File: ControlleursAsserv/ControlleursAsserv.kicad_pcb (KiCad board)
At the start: 2 copper layers, 116 parts, among them J1 I2C1_5, J10 Codeur, J11 Motor FeedBack, J12 Motor CMD, J13 Codeur, J14 Motor FeedBack, J15 Motor CMD, J16 Codeur, J17 Motor FeedBack, J18 Motor CMD, J2 I2C2_5, J3 CAN1, J4 CAN2, J5 In App Prog, J6 DEBUG, J7 Codeur, J8 Motor CMD, J9 Motor FeedBack, Q1 BSS138, Q10 BSS138, Q11 BSS138, Q12 BSS138, Q13 BSS138, Q14 BSS138, Q2 BSS138, Q3 BSS138, Q4 BSS138, Q5 BSS138, Q6 BSS138, Q7 BSS138, Q8 BSS138, Q9 BSS138, SW1 RESET, SW2 BOOT0, U1 STM32G474RETx, U2 AMS1117-3.3, U3 MCP2558FD-xSN, Y1 16MHz

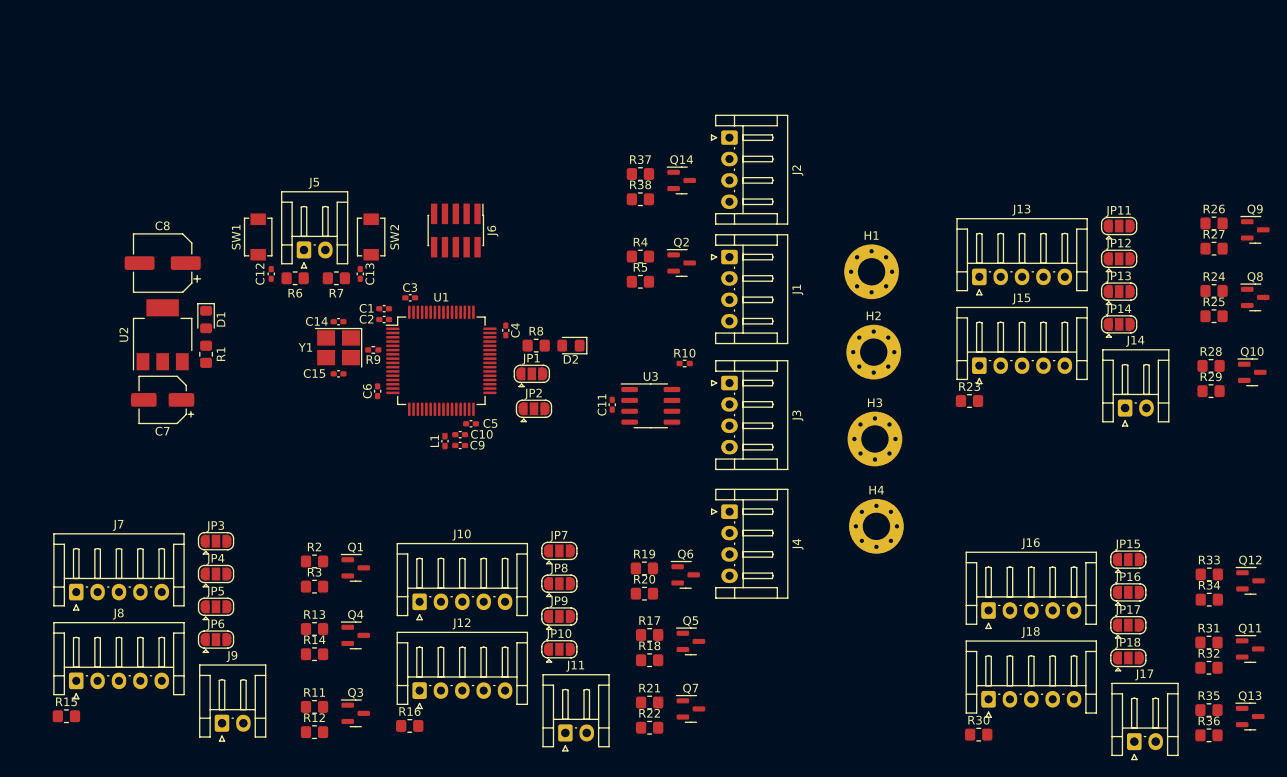
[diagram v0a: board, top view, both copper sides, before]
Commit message: Finalize placement for AsservController
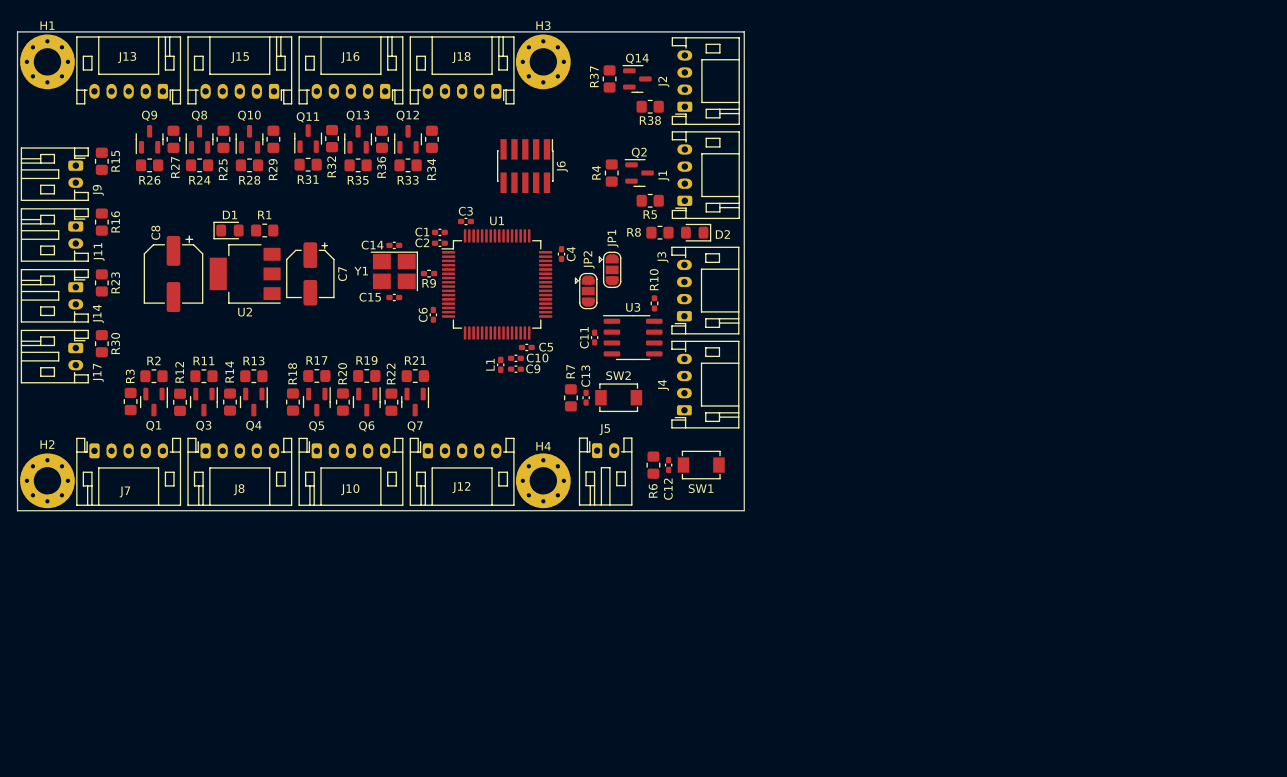
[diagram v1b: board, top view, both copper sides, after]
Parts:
- removed JP10, JP14, JP18, JP3: alim selector, Jumper:SolderJumper-3_P1.3mm_Open_RoundedPad1.0x1.5mm
- removed JP11, JP15, JP4, JP7: CHA Selector, Jumper:SolderJumper-3_P1.3mm_Open_RoundedPad1.0x1.5mm
- removed JP12, JP16, JP5, JP8: CHB Selector, Jumper:SolderJumper-3_P1.3mm_Open_RoundedPad1.0x1.5mm
- removed JP13, JP17, JP6, JP9: IDX Selector, Jumper:SolderJumper-3_P1.3mm_Open_RoundedPad1.0x1.5mm
- J1, J2, J3, J4: footprint Connector_JST:JST_EH_S4B-EH_1x04_P2.50mm_Horizontal -> Connector_JST:JST_PH_S4B-PH-K_1x04_P2.00mm_Horizontal
- J10, J12, J13, J15, J16, J18, J7, J8: footprint Connector_JST:JST_EH_S5B-EH_1x05_P2.50mm_Horizontal -> Connector_JST:JST_PH_S5B-PH-K_1x05_P2.00mm_Horizontal
- J11, J14, J17, J5, J9: footprint Connector_JST:JST_EH_S2B-EH_1x02_P2.50mm_Horizontal -> Connector_JST:JST_PH_S2B-PH-K_1x02_P2.00mm_Horizontal
- moved J17 132.1 mm to (67.6, 75.7), turned to -90 degrees
- moved Q9 129.7 mm to (76.2, 51.3), turned to 90 degrees
- moved Q11 125.3 mm to (94.7, 51.2), turned to 90 degrees
- moved Q8 124.9 mm to (82.0, 51.3), turned to 90 degrees
- moved R26 124.7 mm to (76.2, 54.4)
- moved Q13 124.3 mm to (100.6, 51.3), turned to 90 degrees
- moved J14 123.5 mm to (67.6, 68.6), turned to -90 degrees
- moved R27 122.4 mm to (79.0, 51.3), turned to 90 degrees
- moved Q10 120.4 mm to (87.9, 51.3), turned to 90 degrees
- moved R32 119.8 mm to (97.5, 51.2), turned to 90 degrees
- moved R24 119.6 mm to (82.0, 54.4)
- moved R31 119.3 mm to (94.7, 54.3)
- moved R36 119.2 mm to (103.4, 51.3), turned to 90 degrees
- moved R35 118.2 mm to (100.6, 54.4)
- moved R25 117.7 mm to (84.8, 51.3), turned to 90 degrees
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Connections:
- J10 pad 1: Net-(J10-Pin_1) -> +5V
- J13 pad 1: Net-(J13-Pin_1) -> +5V
- J16 pad 1: Net-(J16-Pin_1) -> +5V
- J7 pad 1: Net-(J7-Pin_1) -> +5V
- Q1 pad 2: /Codeur_Moteur_1/CHA Shifter/LV -> CHA_1
- Q10 pad 2: /Codeur_Moteur_3/CHA Shifter/LV -> CHA_3
- Q11 pad 2: /Codeur_Moteur_4/IDX Shifter/LV -> IDX_4
- Q12 pad 2: /Codeur_Moteur_4/CHA Shifter/LV -> CHA_4
- Q13 pad 2: /Codeur_Moteur_4/CHB Shifter/LV -> CHB_4
- Q3 pad 2: /Codeur_Moteur_1/CHB Shifter/LV -> CHB_1
- Q4 pad 2: /Codeur_Moteur_1/IDX Shifter/LV -> IDX_1
- Q5 pad 2: /Codeur_Moteur_2/CHA Shifter/LV -> CHA_2
- Q6 pad 2: /Codeur_Moteur_2/CHB Shifter/LV -> CHB_2
- Q7 pad 2: /Codeur_Moteur_2/IDX Shifter/LV -> IDX_2
- Q8 pad 2: /Codeur_Moteur_3/CHB Shifter/LV -> CHB_3
- Q9 pad 2: /Codeur_Moteur_3/IDX Shifter/LV -> IDX_3
- R11 pad 2: /Codeur_Moteur_1/CHB Shifter/LV -> CHB_1
- R13 pad 2: /Codeur_Moteur_1/IDX Shifter/LV -> IDX_1
- R17 pad 2: /Codeur_Moteur_2/CHA Shifter/LV -> CHA_2
- R19 pad 2: /Codeur_Moteur_2/CHB Shifter/LV -> CHB_2
- R2 pad 2: /Codeur_Moteur_1/CHA Shifter/LV -> CHA_1
- R21 pad 2: /Codeur_Moteur_2/IDX Shifter/LV -> IDX_2
- R24 pad 2: /Codeur_Moteur_3/CHB Shifter/LV -> CHB_3
- R26 pad 2: /Codeur_Moteur_3/IDX Shifter/LV -> IDX_3
- R28 pad 2: /Codeur_Moteur_3/CHA Shifter/LV -> CHA_3
- R31 pad 2: /Codeur_Moteur_4/IDX Shifter/LV -> IDX_4
- R33 pad 2: /Codeur_Moteur_4/CHA Shifter/LV -> CHA_4
- R35 pad 2: /Codeur_Moteur_4/CHB Shifter/LV -> CHB_4
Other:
- board outline added: 85 x 56 mm

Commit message: Init routing
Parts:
- moved Q1 2.33 mm to (77.2, 79.8)
- moved Q3 2.33 mm to (83.1, 79.8)
- moved Q4 2.33 mm to (88.9, 79.8)
- moved Q5 2.33 mm to (96.3, 79.8)
- moved Q6 2.33 mm to (102.1, 79.8)
- moved Q7 2.33 mm to (107.8, 79.8)
- moved R11 2.33 mm to (83.1, 76.8)
- moved R12 2.33 mm to (80.3, 79.8)
- moved R13 2.33 mm to (88.9, 76.8)
- moved R14 2.33 mm to (86.1, 79.8)
- moved R17 2.33 mm to (96.3, 76.7)
- moved R18 2.33 mm to (93.5, 79.8)
- moved R19 2.33 mm to (102.1, 76.7)
- moved R2 2.33 mm to (77.2, 76.8)
- moved R20 2.33 mm to (99.3, 79.8)
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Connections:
- U1 pad 2: DIR_1 -> DIR_3
- U1 pad 22: SLEEP_3 -> SLEEP_1
- U1 pad 24: SLEEP_1 -> SLEEP_3
- U1 pad 4: DIR_3 -> DIR_1
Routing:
- net +3.3V: track 0.00 -> 73.3 mm, vias 0 -> 18
- net SDA_33: track 0.00 -> 29.6 mm, vias 0 -> 2
- net SCL_5: track 0.00 -> 21.2 mm
- net Net-(J3-Pin_3): track 0.00 -> 20.8 mm
- net SDA_5: track 0.00 -> 20.6 mm
- net SCL_33: track 0.00 -> 19.4 mm
- net Net-(J3-Pin_2): track 0.00 -> 19.4 mm
- net HEART_BEAT: track 0.00 -> 17.9 mm
- net /Codeur_Moteur_3/CHA Shifter/HV: track 0.00 -> 17.6 mm
- net /Codeur_Moteur_1/IDX Shifter/HV: track 0.00 -> 16.4 mm
- net RX_CAN: track 0.00 -> 14.3 mm
- net /Codeur_Moteur_3/CHB Shifter/HV: track 0.00 -> 13.8 mm
- net +5V: track 0.00 -> 12.6 mm
- net /Codeur_Moteur_1/CHB Shifter/HV: track 0.00 -> 12.3 mm
- net SLEEP_2: track 0.00 -> 12.1 mm
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- added copper zone on In2.Cu, net +3.3V
- added copper zone on In1.Cu, net +5V
- added copper zone on B.Cu, net GND
- added copper zone on F.Cu, net GND
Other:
- copper layers 2 -> 4
- board text added: "In App Prg"

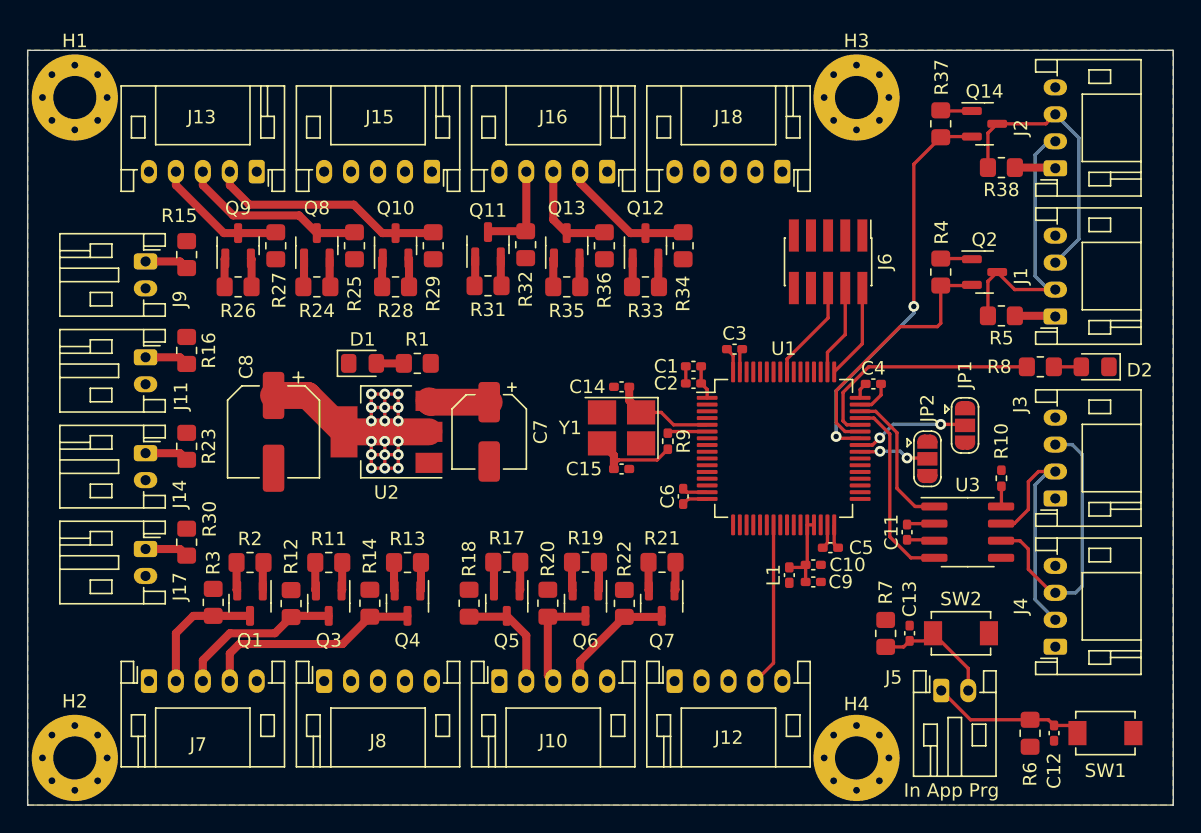
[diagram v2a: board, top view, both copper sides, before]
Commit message: Add routing on controller asserv
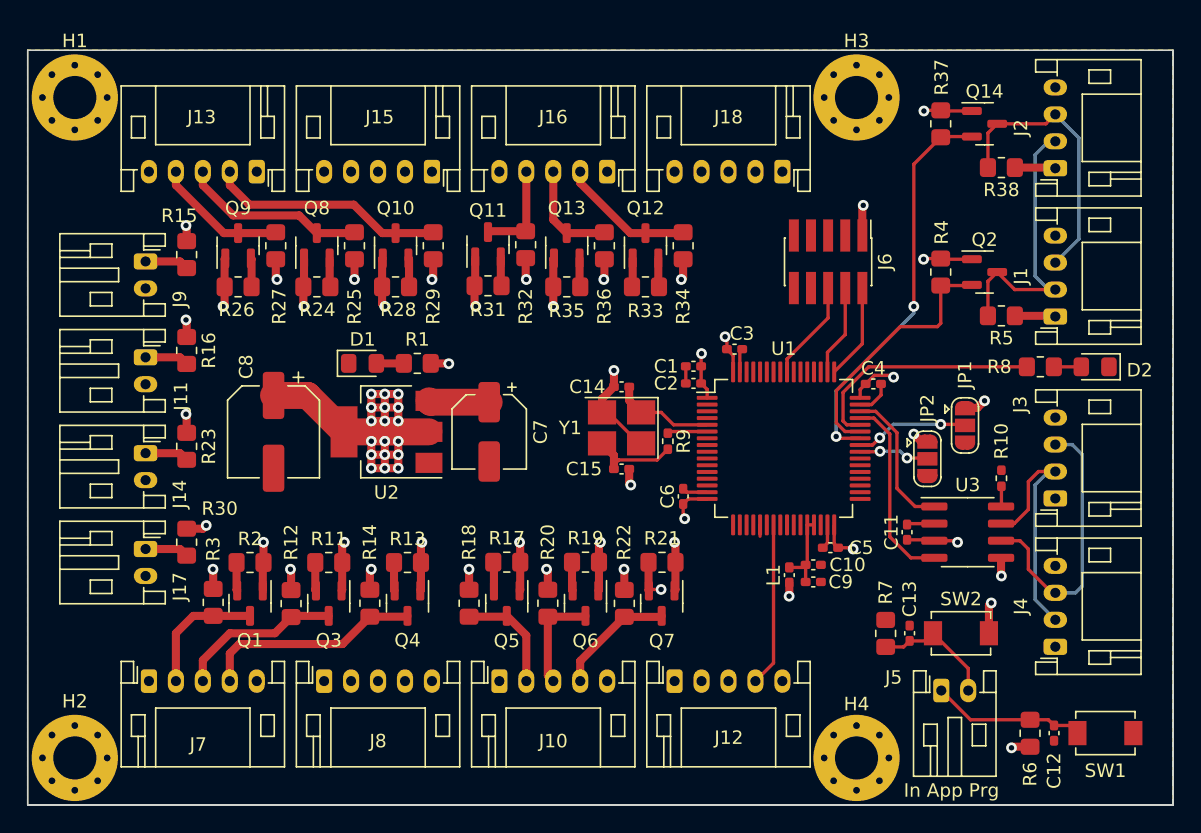
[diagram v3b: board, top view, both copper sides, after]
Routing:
- net +3.3V: track 73.3 -> 120.2 mm, vias 18 -> 48
- net +5V: track 12.6 -> 32.9 mm, vias 0 -> 13
- net GND: track 11.5 -> 20.0 mm, vias 0 -> 2
- net IDX_2: track 2.11 -> 3.05 mm, vias 0 -> 1
- net CHB_2: track 2.13 -> 2.97 mm

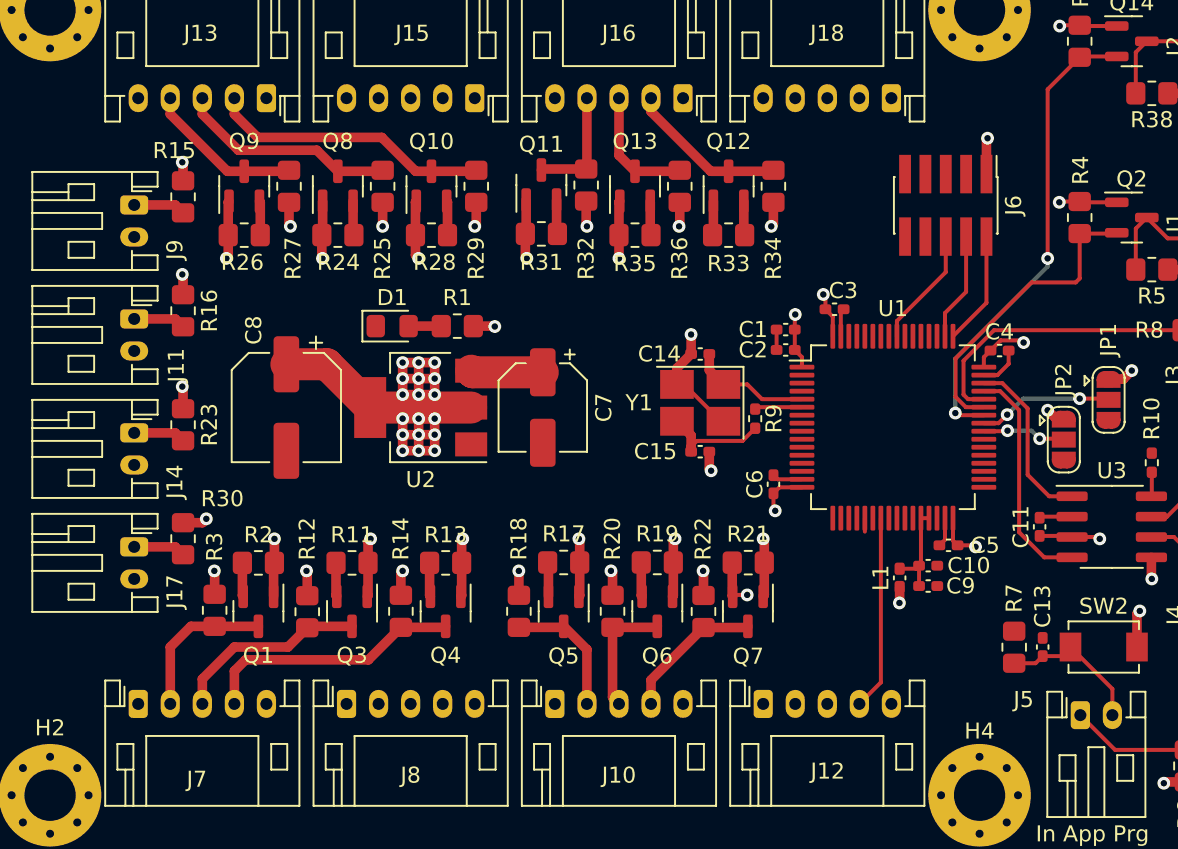
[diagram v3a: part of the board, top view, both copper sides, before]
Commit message: Add some routes to ControlleursAsserv
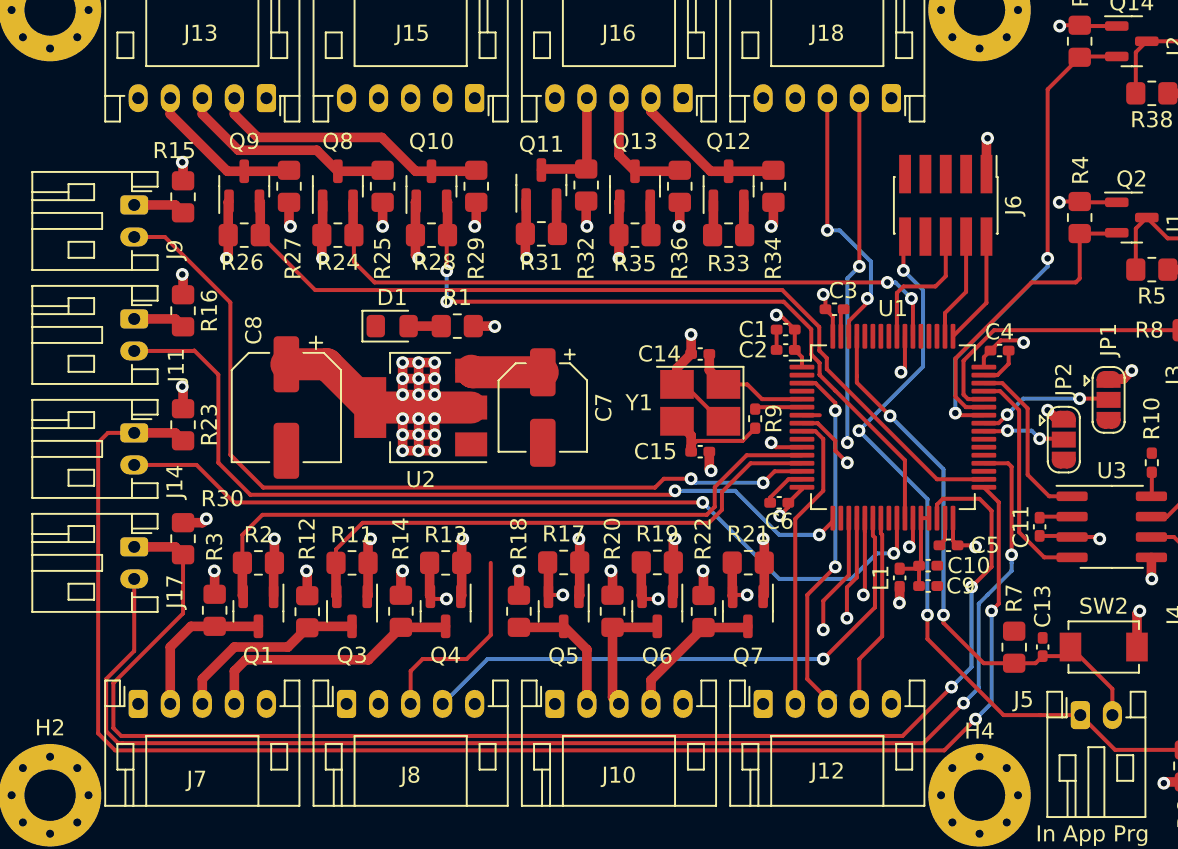
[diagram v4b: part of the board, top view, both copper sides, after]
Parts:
- moved C6 1.21 mm to (109.8, 73.0), turned to 180 degrees
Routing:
- net FAULT_3: track 3.25 -> 95.3 mm, vias 0 -> 2
- net FAULT_4: track 3.25 -> 86.4 mm, vias 0 -> 2
- net CS_4: track 0.00 -> 82.9 mm, vias 0 -> 2
- net CS_1: track 0.00 -> 54.3 mm, vias 0 -> 2
- net CS_3: track 0.00 -> 53.3 mm, vias 0 -> 2
- net IDX_3: track 2.13 -> 54.9 mm
- net CS_2: track 0.00 -> 52.3 mm, vias 0 -> 2
- net PWM_1: track 0.00 -> 43.2 mm, vias 0 -> 1
- net CHA_3: track 2.13 -> 44.0 mm, vias 0 -> 2
- net RESET: track 11.4 -> 53.1 mm, vias 0 -> 3
- net CHB_3: track 2.13 -> 41.9 mm, vias 0 -> 2
- net CHA_1: track 2.11 -> 41.6 mm
- net SLEEP_1: track 0.00 -> 35.1 mm, vias 0 -> 1
- net IDX_1: track 2.11 -> 35.1 mm, vias 0 -> 2
- net CHB_1: track 2.11 -> 34.9 mm
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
